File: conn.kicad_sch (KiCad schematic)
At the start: 12 parts, among them J7 6100.3300.33

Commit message: Updated Acc. parts
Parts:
- added Bcksh1: UT010AC, symbol JP_3xCarbide:Bcksh_/_Clamp
- added PIN1: RM16M23K, symbol JP_3xCarbide:PIN
- added PLUG: UT06104SH, symbol JP_3xCarbide:CONN_UT00104SH(F)
- added Socket1: RC16M23D28, symbol JP_3xCarbide:Socket
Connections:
- net at TB4. (D): now also PTJP5.2
- no-connect marks 17 -> 21
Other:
- note added: "PARTIAL_LASER_STOP(X13.9-21): Current-loop (5V, 40 mA max.)"
- note added: "Ref. CONN of the AOM chassis"
- note added: "SSR,52511"
- note removed: "PARTIAL_LASER_STOP(X13.9-21): Current-loop (5V, 40 mA max.) SYSTEM_STATUE(XS13.19-1): TTL OUT(5V,50mA max.)"
- note removed: "Permit Removal PB"

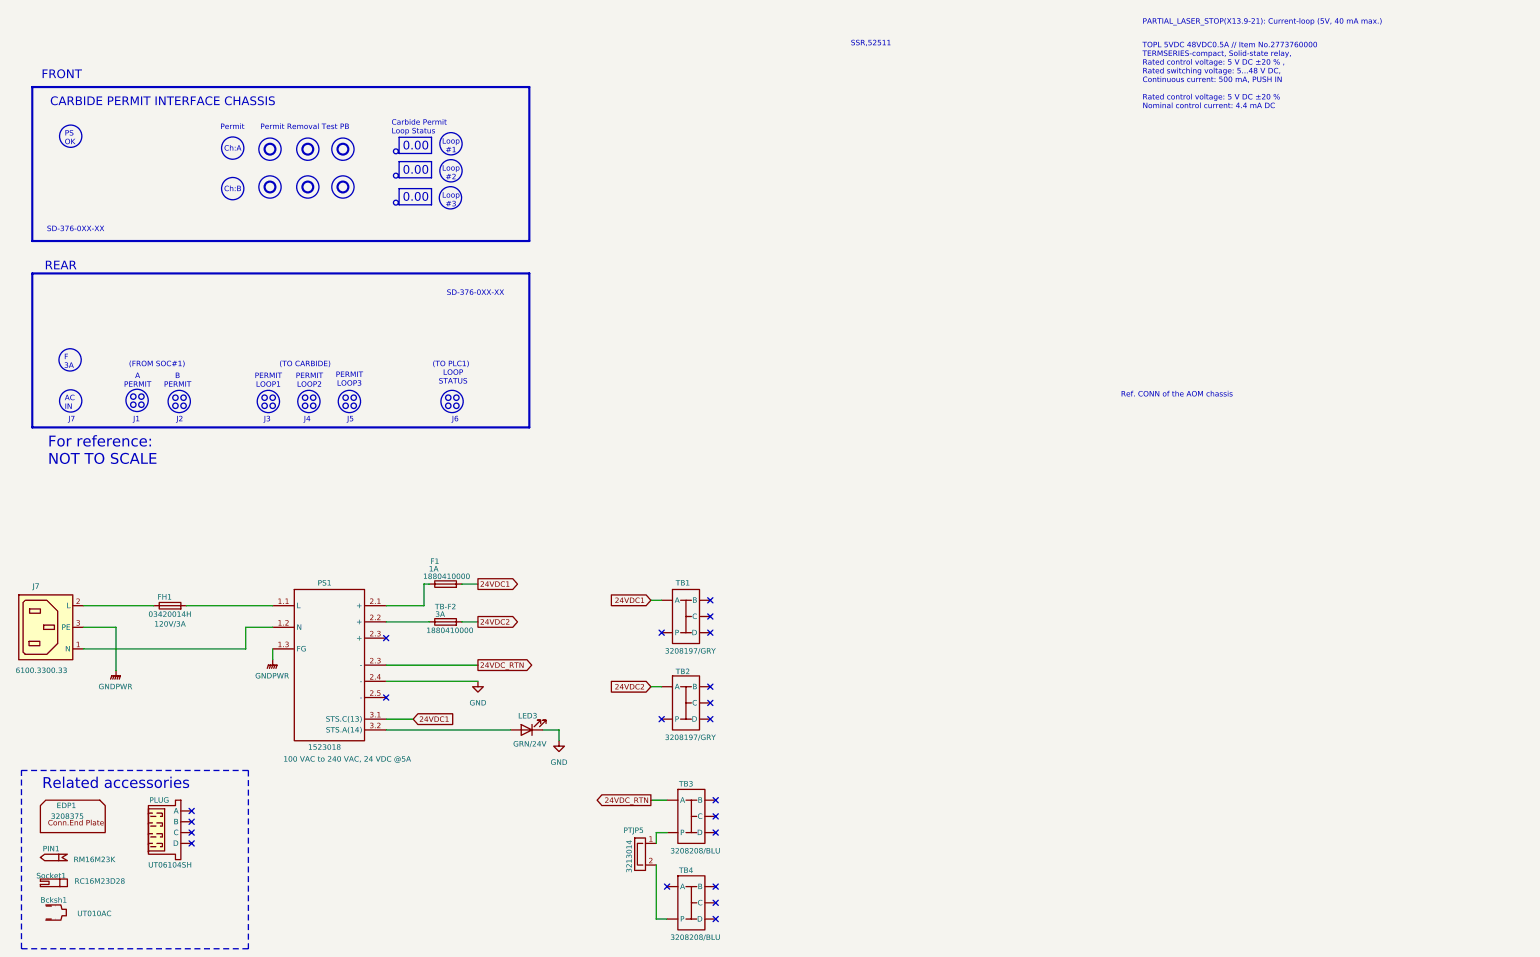
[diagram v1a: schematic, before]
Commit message: Added Interface Cable and etc
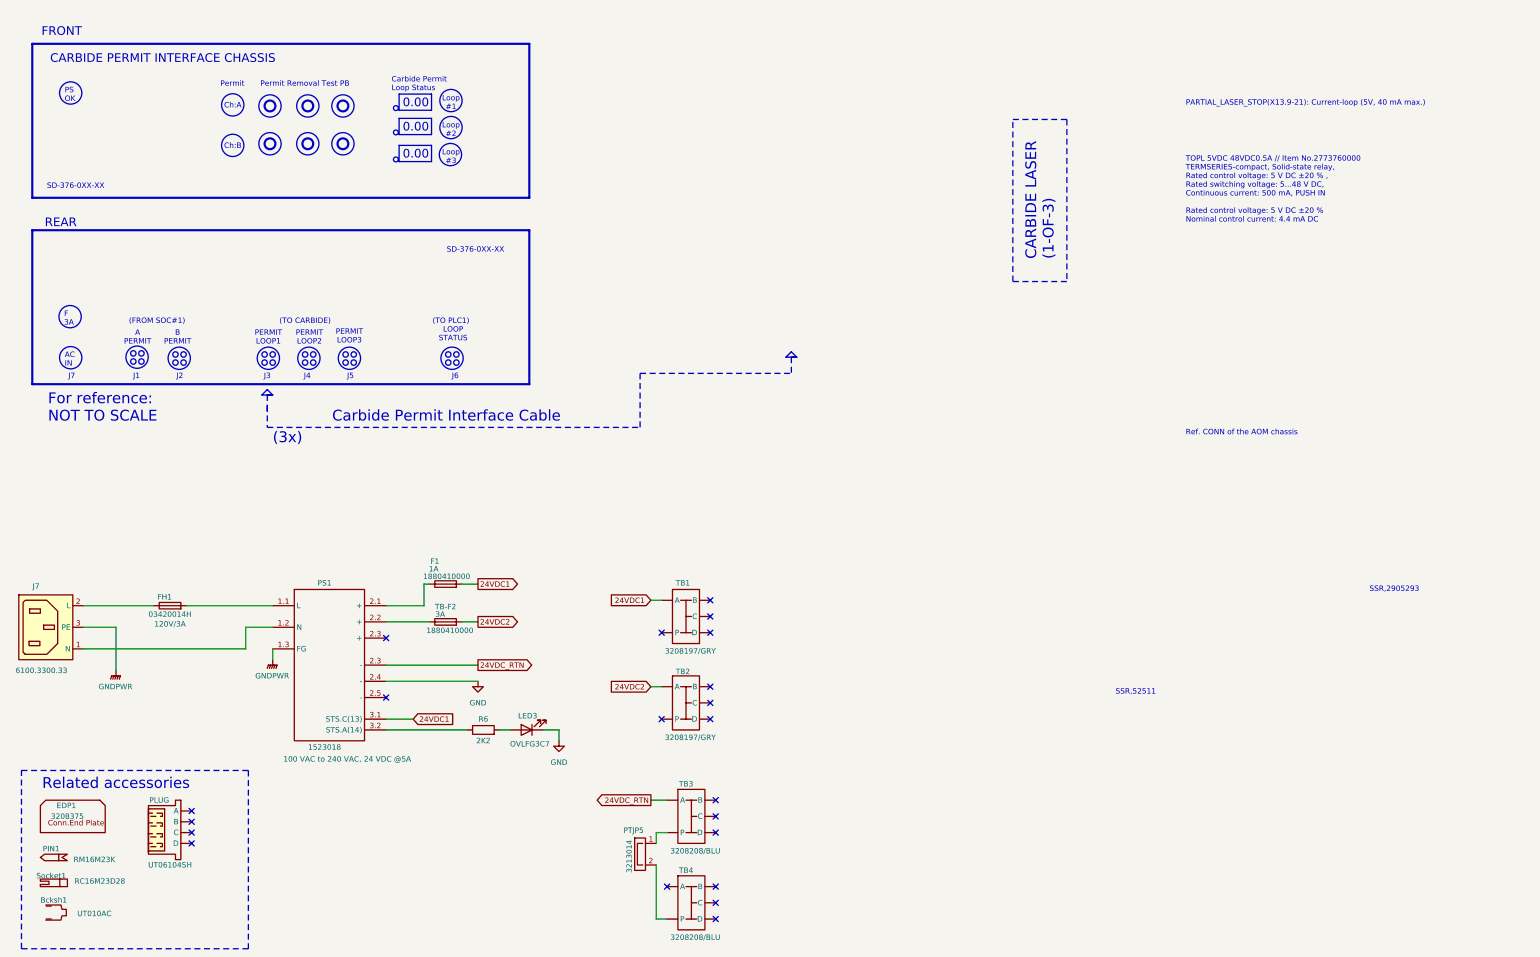
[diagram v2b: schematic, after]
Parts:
- added R6: 2K2, symbol Device:R
- LED3: value GRN/24V -> OVLFG3C7; Info (none) -> Green 525nm LED Indication - Discrete 3.4V Radial
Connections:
- net at TB4. (D): now also PTJP5.2
- net at PS1.3.2 (STS.A(14)): now also R6.1; no longer LED3.2 (A)
- new net: LED3.2 (A), R6.2
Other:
- note added: "(3x)"
- note added: "CARBIDE LASER (1-OF-3)"
- note added: "Carbide Permit Interface Cable"
- note added: "SSR,2905293"

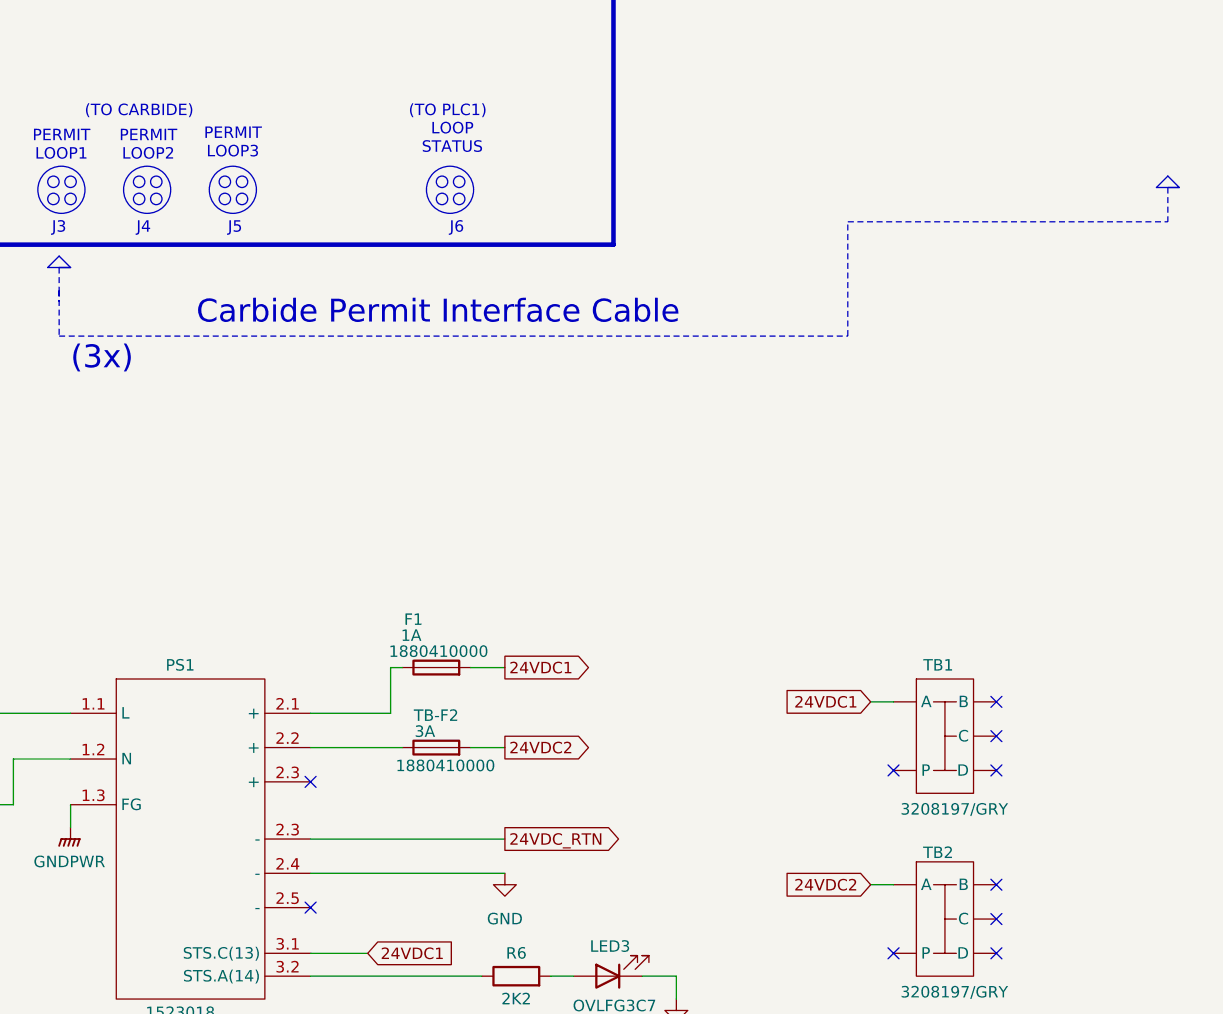
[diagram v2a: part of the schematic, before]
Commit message: Updated Interface cable
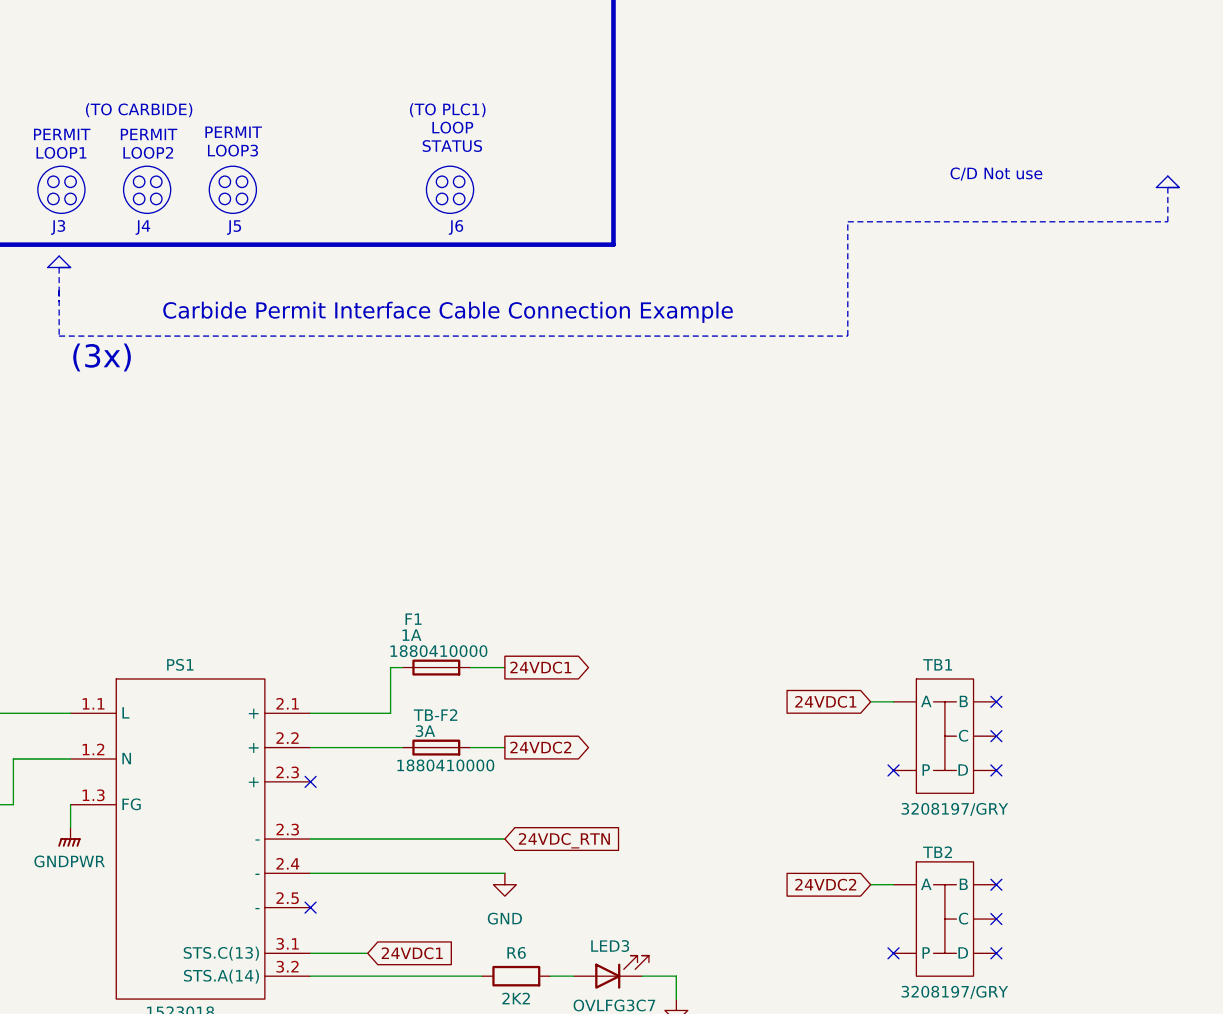
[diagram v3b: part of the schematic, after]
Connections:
- net at TB4. (D): now also PTJP5.2
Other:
- note added: "C/D Not use"
- note added: "Carbide Permit Interface Cable Connection Example"
- note removed: "Carbide Permit Interface Cable"
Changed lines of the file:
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@@
 		)
 	)
+	(text "C/D Not use"
+		(exclude_from_sim no)
+		(at 217.17 111.76 0)
+		(effects
+			(font
+				(size 1.27 1.27)
+			)
+		)
+	)
 	(text "J1"
 		(exclude_from_sim no)
@@
 		)
 	)
-	(text "Carbide Permit Interface Cable"
+	(text "Carbide Permit Interface Cable Connection Example"
 		(exclude_from_sim no)
-		(at 128.27 127 0)
+		(at 124.46 127 0)
 		(effects
 			(font
-				(size 2.54 2.54)
+				(size 1.778 1.778)
 			)
 			(justify left)
@@
 	)
 	(global_label "24VDC_RTN"
-		(shape output)
+		(shape input)
 		(at 162.56 185.42 0)
 		(fields_autoplaced yes)

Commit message: Clean up
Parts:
- renumbered Bcksh1 to Acc.Bcksh1, EDP1 to Acc.EDP1, PIN1 to Acc.PIN1, PLUG to Acc.PLUG, Socket1 to Acc.Socket1
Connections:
- net at TB4. (D): now also PTJP5.2
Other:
- note added: "Key SSR -Switch off characteristics"
- note added: "SSR(20KhZ),52511 Switch off delay max. 18 µs"
- note added: "SSR,2905293 Typical turn-off time 300 µs"
- note removed: "SSR,2905293"
- note removed: "SSR,52511"
- moved on the sheet: Acc.EDP1
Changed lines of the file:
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@@
 		)
 	)
+	(rectangle
+		(start 312.42 167.64)
+		(end 410.21 229.87)
+		(stroke
+			(width 0)
+			(type dash)
+		)
+		(fill
+			(type none)
+		)
+	)
 	(circle
 		(center 155.575 114.3)
@@
 	(text "Ref. CONN of the AOM chassis"
 		(exclude_from_sim no)
-		(at 328.93 130.81 0)
+		(at 323.85 130.81 0)
 		(effects
 			(font
@@
 		)
 	)
-	(text "SSR,2905293"
+	(text "SSR,2905293\nTypical turn-off time 300 µs"
 		(exclude_from_sim no)
-		(at 372.11 167.64 0)
+		(at 367.03 176.53 0)
 		(effects
 			(font
@@
 		)
 	)
+	(text "Key SSR \n-Switch off characteristics"
+		(exclude_from_sim no)
+		(at 314.96 173.99 0)
+		(effects
+			(font
+				(size 2.032 2.032)
+			)
+			(justify left)
+		)
+	)
 	(text "PERMIT\nLOOP1"
 		(exclude_from_sim no)
@@
 		)
 	)
-	(text "SSR,52511"
+	(text "SSR(20KhZ),52511\nSwitch off delay max. 18 µs"
 		(exclude_from_sim no)
-		(at 312.42 191.77 0)
+		(at 316.23 196.85 0)
 		(effects
 			(font
@@
 	)
 	(image
-		(at 334.01 208.28)
+		(at 337.82 213.36)
 		(scale 0.211784)
 		(data "iVBORw0KGgoAAAANSUhEUgAAAuQAAAH+CAIAAABbY4xSAAAAA3NCSVQICAjb4U/gAAAACXBIWXMA"
@@
 	)
 	(image
-		(at 392.43 196.85)
-		(scale 0.326628)
+		(at 384.81 203.2)
+		(scale 0.273804)
 		(data "iVBORw0KGgoAAAANSUhEUgAAAd4AAAJsCAYAAABTdMIgAAAAAXNSR0IArs4c6QAAAARnQU1BAACx"
 			"jwv8YQUAAAAJcEhZcwAADsMAAA7DAcdvqGQAAP+lSURBVHhe7L0FeBzHtrZ77v0P3f+cvc8+G5Md"
@@
 	)
 	(image
-		(at 370.205 142.875)
+		(at 365.125 142.875)
 		(scale 0.0893087)
 		(data "/9j/4AAQSkZJRgABAQEASABIAAD/2wBDAAMCAgMCAgMDAwMEAwMEBQgFBQQEBQoHBwYIDAoMDAsK"
@@
 	(symbol
 		(lib_id "JP_3xCarbide:TB-End")
-		(at 76.2 219.71 0)
+		(at 76.2 220.98 0)
 		(unit 1)
 		(body_style 1)
@@
 		(in_pos_files yes)
 		(dnp no)
-		(property "Reference" "EDP1"
-			(at 63.5 218.44 0)
+		(property "Reference" "Acc.EDP1"
+			(at 62.23 217.17 0)
 			(show_name no)
 			(do_not_autoplace no)
@@
 		)
 		(property "Footprint" ""
-			(at 76.2 219.71 0)
+			(at 76.2 220.98 0)
 			(hide yes)
 			(show_name no)
@@
 		)
 		(property "Datasheet" "https://www.phoenixcontact.com/en-us/products/end-cover-d-pt-15s-quattro-3208375?type=pdf"
-			(at 76.2 219.71 0)
+			(at 76.2 220.98 0)
 			(hide yes)
 			(show_name no)
@@
 		)
 		(property "Description" "Connector End Plate For CLIPLINE PT Series"
-			(at 76.2 219.71 0)
+			(at 76.2 220.98 0)
 			(hide yes)
 			(show_name no)
@@
 		)
 		(property "Mfr" "Phoenix Contact"
-			(at 76.2 219.71 0)
+			(at 76.2 220.98 0)
 			(hide yes)
 			(show_name no)
@@
 		)
 		(property "Cost" "$0.84"
-			(at 76.2 219.71 0)
+			(at 76.2 220.98 0)
 			(hide yes)
 			(show_name no)
@@
 			(project "3xCarbide Permit ILK"
 				(path "/224bdcb2-225d-496a-8b41-82b301326953"
-					(reference "EDP1")
+					(reference "Acc.EDP1")
 					(unit 1)
 				)
@@
 		(in_pos_files yes)
 		(dnp no)
-		(property "Reference" "Socket1"
-			(at 62.23 234.95 0)
+		(property "Reference" "Acc.Socket1"
+			(at 64.77 234.95 0)
 			(show_name no)
 			(do_not_autoplace no)
@@
 			(project "3xCarbide Permit ILK"
 				(path "/224bdcb2-225d-496a-8b41-82b301326953"
-					(reference "Socket1")
+					(reference "Acc.Socket1")
 					(unit 1)
 				)
@@
 		(in_pos_files yes)
 		(dnp no)
-		(property "Reference" "PLUG"
-			(at 87.63 217.17 0)
+		(property "Reference" "Acc.PLUG"
+			(at 86.36 217.17 0)
 			(show_name no)
 			(do_not_autoplace no)
@@
 			(project "3xCarbide Permit ILK"
 				(path "/224bdcb2-225d-496a-8b41-82b301326953"
-					(reference "PLUG")
+					(reference "Acc.PLUG")
 					(unit 1)
 				)
@@
 		(in_pos_files yes)
 		(dnp no)
-		(property "Reference" "Bcksh1"
+		(property "Reference" "Acc.Bcksh1"
 			(at 59.69 240.665 0)
 			(show_name no)
@@
 			(project "3xCarbide Permit ILK"
 				(path "/224bdcb2-225d-496a-8b41-82b301326953"
-					(reference "Bcksh1")
+					(reference "Acc.Bcksh1")
 					(unit 1)
 				)
@@
 		(in_pos_files yes)
 		(dnp no)
-		(property "Reference" "PIN1"
-			(at 62.23 228.6 0)
+		(property "Reference" "Acc.PIN1"
+			(at 63.5 228.6 0)
 			(show_name no)
 			(do_not_autoplace no)
@@
 			(project "3xCarbide Permit ILK"
 				(path "/224bdcb2-225d-496a-8b41-82b301326953"
-					(reference "PIN1")
+					(reference "Acc.PIN1")
 					(unit 1)
 				)

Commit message: Updated PS and clean up
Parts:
- removed F1: 1880410000, symbol Device:Fuse
- added PTJP6: 3213014, symbol JP_3xCarbide:JPTB
- PS1: value 1523018 -> RWS100B-24; Cost $138.29 -> $62.37; Info 100 VAC to 240 VAC, 24 VDC @5A -> 100 VAC to 240 VAC, 24 VDC @4.5A; Mfr Phoenix Cont -> TDK-Lambda
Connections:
- net 24VDC_RTN: now also PS1. (V-); no longer PS1.2.3 (-)
- net GND: now also PS1. (V-); no longer PS1.2.4 (-)
- net GNDPWR: now also PS1. (V-); no longer PS1.1.3 (FG)
- net 24VDC: now reaches TB1. (D)
- net 24VDC: now also R6.1, TB-F2.2
- net at TB4. (D): now also PTJP5.2
- net at TB-F2.1: now also PS1. (V-); no longer PS1.2.2 (+)
- net at FH1.2: now also PS1. (V-); no longer PS1.1.1 (L)
- net at J7.1 (N): now also PS1. (V-); no longer PS1.1.2 (N)
- removed net 24VDC1: PS1.3.1 (STS.C(13)), TB1. (D)
- removed net 24VDC2: TB-F2.2, TB2. (D)
- new net: PTJP6.1, TB1. (D)
- new net: PTJP6.2, TB2. (D)
- no-connect marks 21 -> 19
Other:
- moved on the sheet: LED3, R6, TB-F2

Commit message: updated SSR Pin and cleanup
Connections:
- net at TB4. (D): now also PTJP5.2
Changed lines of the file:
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@@
 		(title "LCLS-II BCS CARBIDE PERMIT INTERLOCK")
 		(date "2026-08-21")
-		(rev "1.02")
+		(rev "1.03")
 		(company "SLAC")
 		(comment 1 "ENGR: J.Park")

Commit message: added diode on MURR SSR
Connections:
- net at TB4. (D): now also PTJP5.2
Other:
- note added: "A/B Not use"
- note removed: "C/D Not use"
